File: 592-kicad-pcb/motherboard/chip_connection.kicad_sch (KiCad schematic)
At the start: 38 parts, among them J3 DF40C-40DP-0.4V(51), J31 Conn_02x01, J4 DF40C-40DP-0.4V(51), U29 74CBTLV3257PW,118, U30 74CBTLV3257PW,118, U31 74CBTLV3257PW,118, U32 74CBTLV3257PW,118

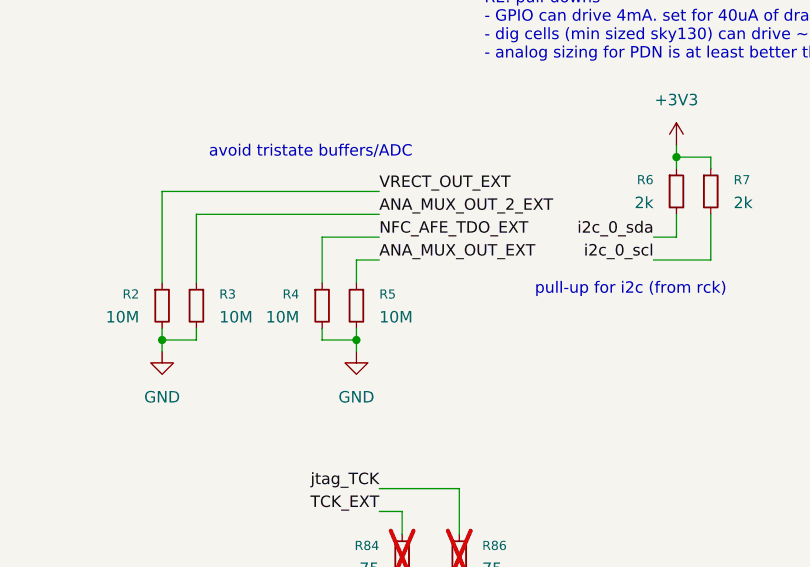
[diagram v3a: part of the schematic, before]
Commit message: add FTDI local routing, muxes
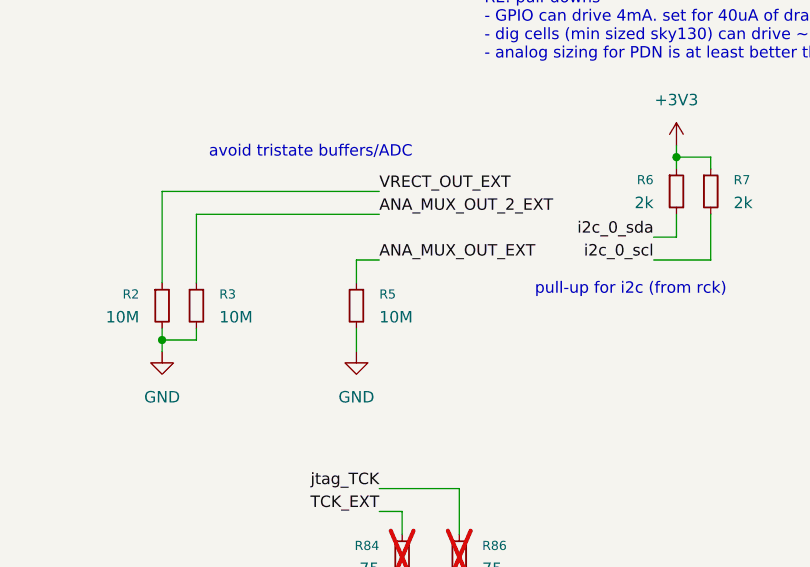
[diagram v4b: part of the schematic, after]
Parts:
- removed R4: 10M, Resistor_SMD:R_0603_1608Metric, symbol Device:R_Small
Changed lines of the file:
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@@
 	)
 	(junction
-		(at 181.61 59.69)
-		(diameter 0)
-		(color 0 0 0 0)
-	)
-	(junction
 		(at 240.03 90.17)
 		(diameter 0)
@@
 	(wire
 		(pts
-			(xy 177.8 48.26) (xy 184.15 48.26)
-		)
-		(stroke
-			(width 0)
-			(type default)
-		)
-	)
-	(wire
-		(pts
 			(xy 307.34 185.42) (xy 309.88 185.42)
 		)
@@
 	(wire
 		(pts
-			(xy 177.8 53.34) (xy 177.8 48.26)
-		)
-		(stroke
-			(width 0)
-			(type default)
-		)
-	)
-	(wire
-		(pts
 			(xy 240.03 99.06) (xy 237.49 99.06)
 		)
@@
 	(wire
 		(pts
-			(xy 181.61 59.69) (xy 181.61 60.96)
-		)
-		(stroke
-			(width 0)
-			(type default)
-		)
-	)
-	(wire
-		(pts
 			(xy 125.73 151.13) (xy 128.27 151.13)
 		)
@@
 	(wire
 		(pts
-			(xy 177.8 59.69) (xy 177.8 58.42)
-		)
-		(stroke
-			(width 0)
-			(type default)
-		)
-	)
-	(wire
-		(pts
 			(xy 30.48 215.9) (xy 30.48 222.25)
 		)
@@
 	(wire
 		(pts
-			(xy 181.61 59.69) (xy 177.8 59.69)
-		)
-		(stroke
-			(width 0)
-			(type default)
-		)
-	)
-	(wire
-		(pts
 			(xy 250.19 46.99) (xy 250.19 57.15)
 		)
@@
 	(wire
 		(pts
-			(xy 181.61 58.42) (xy 181.61 59.69)
+			(xy 181.61 58.42) (xy 181.61 60.96)
 		)
 		(stroke
@@
 		)
 	)
-	(label "NFC_AFE_TDO_EXT"
-		(at 184.15 48.26 0)
-		(effects
-			(font
-				(size 1.27 1.27)
-			)
-			(justify left bottom)
-		)
-	)
 	(label "jtag_TCK"
 		(at 184.15 76.2 180)
@@
 					(unit 1)
 				)
-			)
-		)
-	)
-	(symbol
-		(lib_id "Device:R_Small")
-		(at 177.8 55.88 0)
-		(unit 1)
-		(exclude_from_sim no)
-		(in_bom yes)
-		(on_board yes)
-		(dnp no)
-		(property "Reference" "R4"
-			(at 175.26 54.6099 0)
-			(effects
-				(font
-					(size 1.016 1.016)
-				)
-				(justify right)
-			)
-		)
-		(property "Value" "10M"
-			(at 175.26 57.1499 0)
-			(effects
-				(font
-					(size 1.27 1.27)
-				)
-				(justify right)
-			)
-		)
-		(property "Footprint" "Resistor_SMD:R_0603_1608Metric"
-			(at 177.8 55.88 0)
-			(effects
-				(font
-					(size 1.27 1.27)
-				)
-				(hide yes)
-			)
-		)
-		(property "Datasheet" "~"
-			(at 177.8 55.88 0)
-			(effects
-				(font
-					(size 1.27 1.27)
-				)
-				(hide yes)
-			)
-		)
-		(property "Description" "Resistor, small symbol"
-			(at 177.8 55.88 0)
-			(effects
-				(font
-					(size 1.27 1.27)
-				)
-				(hide yes)
-			)
-		)
-		(property "LCSC" "C7250"
-			(at 177.8 55.88 0)
-			(effects
-				(font
-					(size 1.27 1.27)
-				)
-				(hide yes)
-			)
-		)
-		(property "Characteristics" ""
-			(at 177.8 55.88 0)
-			(effects
-				(font
-					(size 1.27 1.27)
-				)
-				(hide yes)
-			)
-		)
-		(property "DigikeyPN" ""
-			(at 177.8 55.88 0)
-			(effects
-				(font
-					(size 1.27 1.27)
-				)
-				(hide yes)
-			)
-		)
-		(property "MPN" ""
-			(at 177.8 55.88 0)
-			(effects
-				(font
-					(size 1.27 1.27)
-				)
-				(hide yes)
-			)
-		)
-		(property "MPN_ALT" ""
-			(at 177.8 55.88 0)
-			(effects
-				(font
-					(size 1.27 1.27)
-				)
-				(hide yes)
-			)
-		)
-		(property "Manufacturer" ""
-			(at 177.8 55.88 0)
-			(effects
-				(font
-					(size 1.27 1.27)
-				)
-				(hide yes)
-			)
-		)
-		(property "Variant" ""
-			(at 177.8 55.88 0)
-			(effects
-				(font
-					(size 1.27 1.27)
-				)
-				(hide yes)
-			)
-		)
-		(property "Vendor" ""
-			(at 177.8 55.88 0)
-			(effects
-				(font
-					(size 1.27 1.27)
-				)
-				(hide yes)
-			)
-		)
-		(pin "2"
-		)
-		(pin "1"
-		)
-		(instances
-			(project "motherboard"
-				(path "/5b0c97ac-fa03-4db8-b41b-0eee32b6f55d/f049e4ad-bebe-4338-850a-2727de737ae9/f6d635ad-dccc-4a37-acef-12f77d37e99b"
-					(reference "R4")
-					(unit 1)
-				)

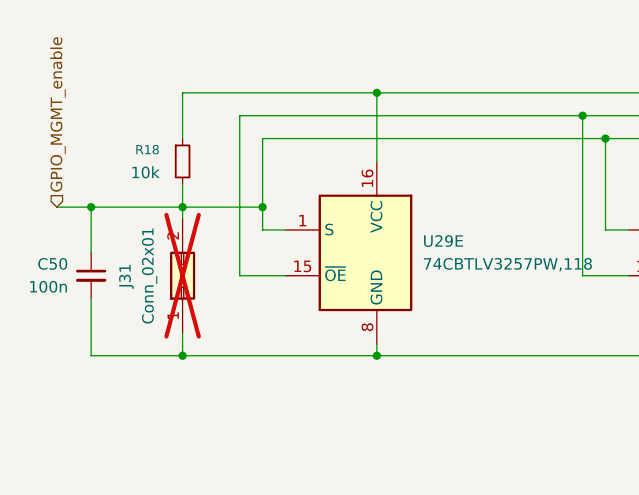
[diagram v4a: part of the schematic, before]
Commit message: complete routing for core
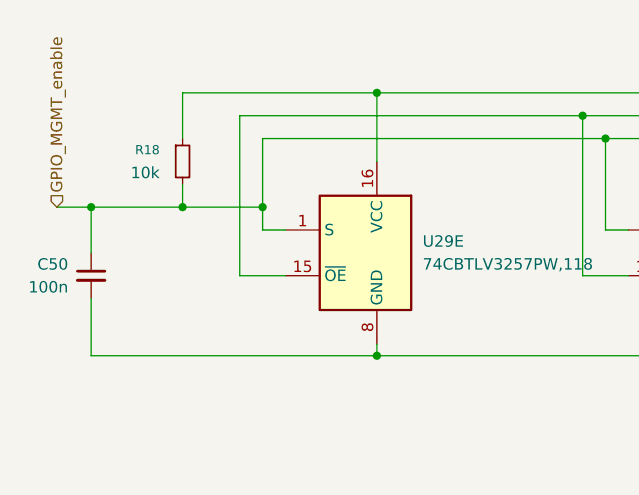
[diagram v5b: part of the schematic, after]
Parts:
- removed J31: Conn_02x01, Connector_PinHeader_1.27mm:PinHeader_1x02_P1.27mm_Vertical, symbol Connector_Generic:Conn_02x01
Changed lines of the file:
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@@
 	)
 	(junction
-		(at 40.64 222.25)
-		(diameter 0)
-		(color 0 0 0 0)
-	)
-	(junction
 		(at 250.19 40.64)
 		(diameter 0)
@@
 	(wire
 		(pts
-			(xy 40.64 207.01) (xy 40.64 205.74)
-		)
-		(stroke
-			(width 0)
-			(type default)
-		)
-	)
-	(wire
-		(pts
 			(xy 62.23 105.41) (xy 64.77 105.41)
 		)
@@
 	(wire
 		(pts
-			(xy 40.64 222.25) (xy 40.64 219.71)
-		)
-		(stroke
-			(width 0)
-			(type default)
-		)
-	)
-	(wire
-		(pts
 			(xy 125.73 140.97) (xy 128.27 140.97)
 		)
@@
 	(wire
 		(pts
-			(xy 40.64 222.25) (xy 62.23 222.25)
+			(xy 30.48 222.25) (xy 62.23 222.25)
 		)
 		(stroke
@@
 	(wire
 		(pts
-			(xy 30.48 222.25) (xy 40.64 222.25)
-		)
-		(stroke
-			(width 0)
-			(type default)
-		)
-	)
-	(wire
-		(pts
 			(xy 273.05 182.88) (xy 275.59 182.88)
 		)
@@
 					(unit 1)
 				)
-			)
-		)
-	)
-	(symbol
-		(lib_id "Connector_Generic:Conn_02x01")
-		(at 40.64 214.63 90)
-		(unit 1)
-		(exclude_from_sim no)
-		(in_bom yes)
-		(on_board yes)
-		(dnp yes)
-		(fields_autoplaced yes)
-		(property "Reference" "J31"
-			(at 34.29 213.36 0)
-			(effects
-				(font
-					(size 1.27 1.27)
-				)
-			)
-		)
-		(property "Value" "Conn_02x01"
-			(at 36.83 213.36 0)
-			(effects
-				(font
-					(size 1.27 1.27)
-				)
-			)
-		)
-		(property "Footprint" "Connector_PinHeader_1.27mm:PinHeader_1x02_P1.27mm_Vertical"
-			(at 40.64 214.63 0)
-			(effects
-				(font
-					(size 1.27 1.27)
-				)
-				(hide yes)
-			)
-		)
-		(property "Datasheet" "~"
-			(at 40.64 214.63 0)
-			(effects
-				(font
-					(size 1.27 1.27)
-				)
-				(hide yes)
-			)
-		)
-		(property "Description" "Generic connector, double row, 02x01, this symbol is compatible with counter-clockwise, top-bottom and odd-even numbering schemes., script generated (kicad-library-utils/schlib/autogen/connector/)"
-			(at 40.64 214.63 0)
-			(effects
-				(font
-					(size 1.27 1.27)
-				)
-				(hide yes)
-			)
-		)
-		(property "Characteristics" ""
-			(at 40.64 214.63 0)
-			(effects
-				(font
-					(size 1.27 1.27)
-				)
-				(hide yes)
-			)
-		)
-		(property "DigikeyPN" ""
-			(at 40.64 214.63 0)
-			(effects
-				(font
-					(size 1.27 1.27)
-				)
-				(hide yes)
-			)
-		)
-		(property "MPN" ""
-			(at 40.64 214.63 0)
-			(effects
-				(font
-					(size 1.27 1.27)
-				)
-				(hide yes)
-			)
-		)
-		(property "MPN_ALT" ""
-			(at 40.64 214.63 0)
-			(effects
-				(font
-					(size 1.27 1.27)
-				)
-				(hide yes)
-			)
-		)
-		(property "Manufacturer" ""
-			(at 40.64 214.63 0)
-			(effects
-				(font
-					(size 1.27 1.27)
-				)
-				(hide yes)
-			)
-		)
-		(property "Variant" ""
-			(at 40.64 214.63 0)
-			(effects
-				(font
-					(size 1.27 1.27)
-				)
-				(hide yes)
-			)
-		)
-		(property "Vendor" ""
-			(at 40.64 214.63 0)
-			(effects
-				(font
-					(size 1.27 1.27)
-				)
-				(hide yes)
-			)
-		)
-		(pin "1"
-		)
-		(pin "2"
-		)
-		(instances
-			(project "motherboard"
-				(path "/5b0c97ac-fa03-4db8-b41b-0eee32b6f55d/f049e4ad-bebe-4338-850a-2727de737ae9/f6d635ad-dccc-4a37-acef-12f77d37e99b"
-					(reference "J31")
-					(unit 1)
-				)
